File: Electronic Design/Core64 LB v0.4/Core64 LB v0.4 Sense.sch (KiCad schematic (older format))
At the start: 23 parts, among them U3 LM393

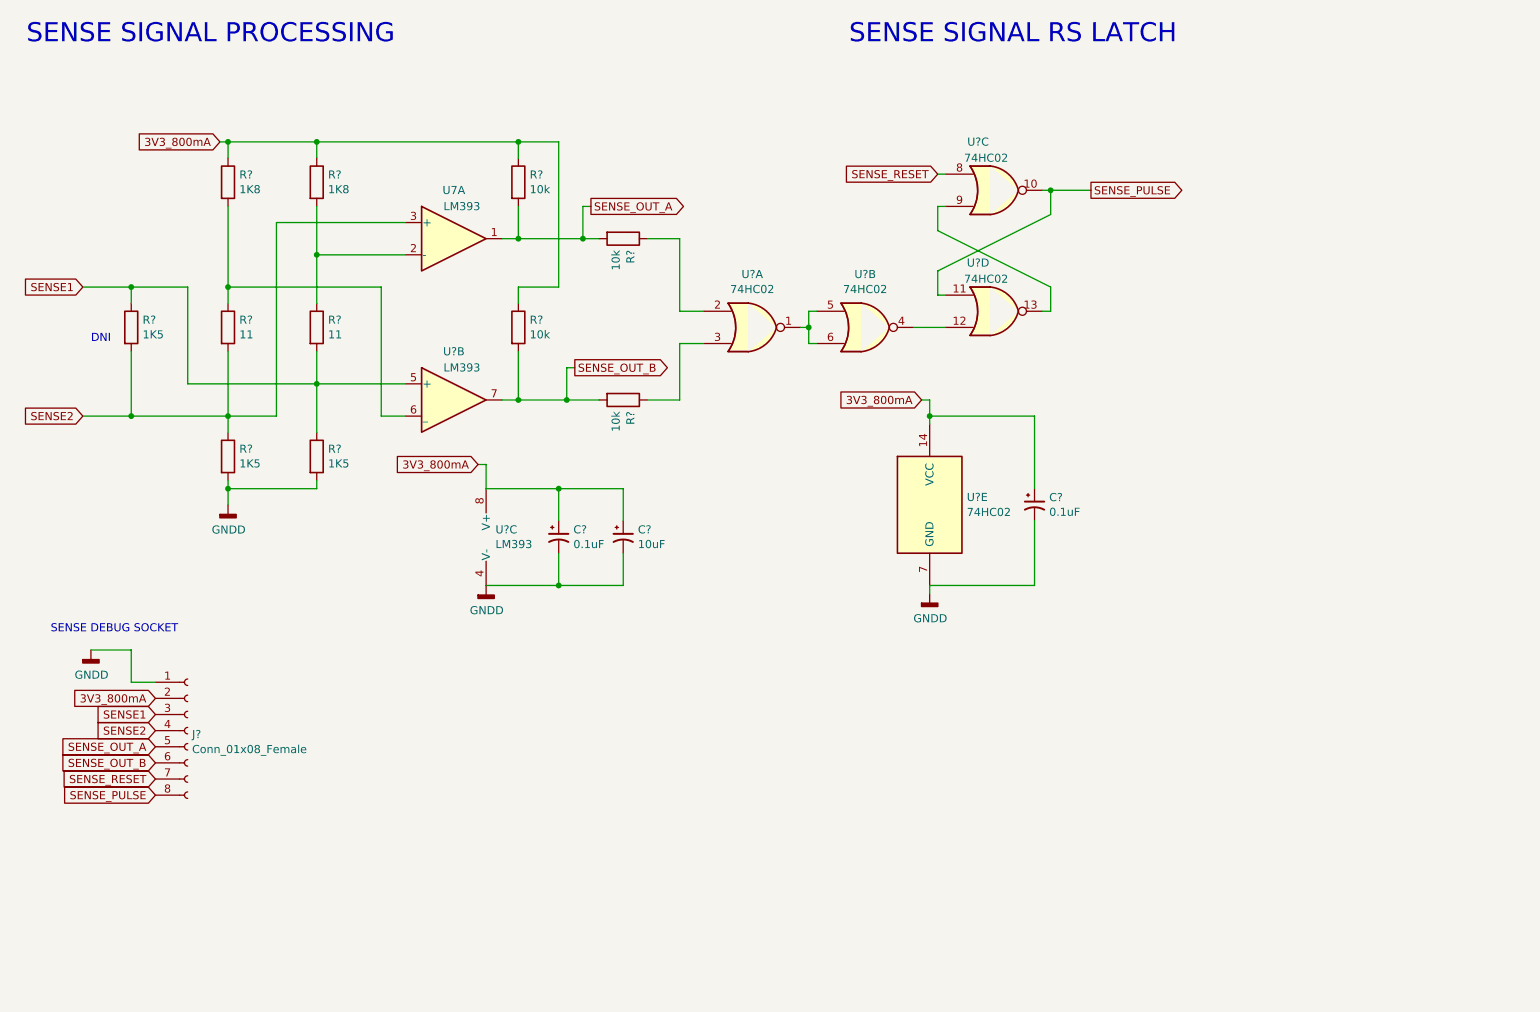
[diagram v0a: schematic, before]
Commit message: Correct Logic Board filenames to LB from CB
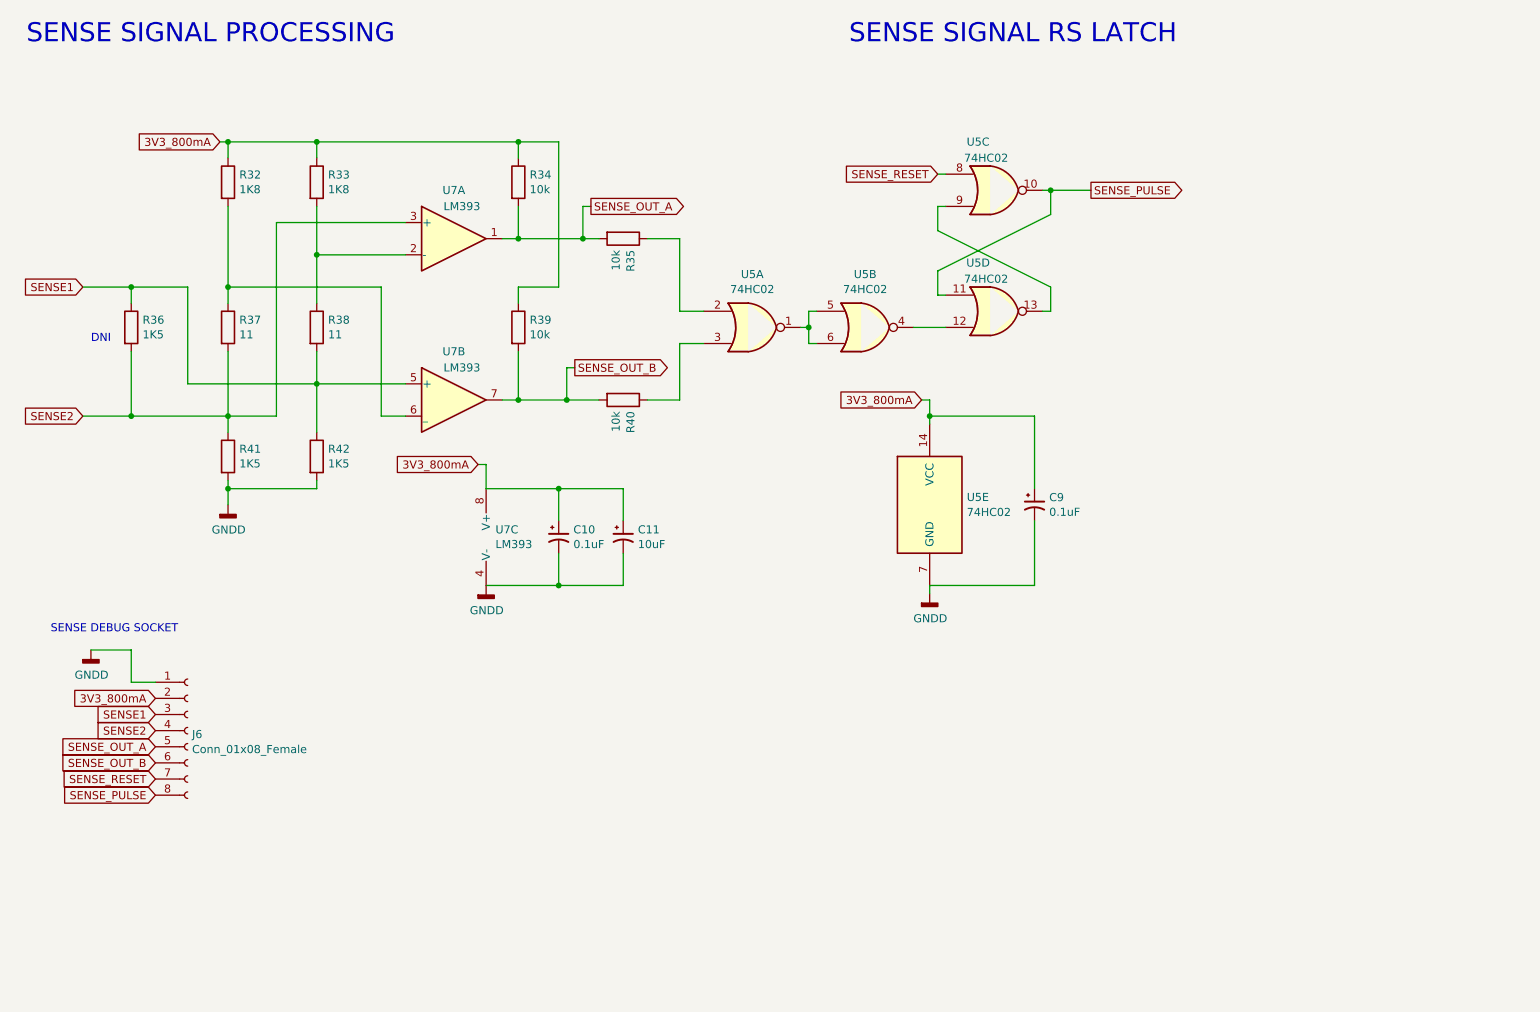
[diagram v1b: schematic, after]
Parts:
- gave numbers to parts that had none: 17
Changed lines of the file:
@@
 EESchema Schematic File Version 4
-LIBS:Core64 CB v0.4-cache
+LIBS:Core64 LB v0.4-cache
 EELAYER 29 0
 EELAYER END
@@
 SENSE2
 $Comp
-L Device:R R?
+L Device:R R32
 U 1 1 5D39C2B1
 P 1850 1700
-F 0 "R?" H 1920 1746 50  0000 L CNN
+F 0 "R32" H 1920 1746 50  0000 L CNN
 F 1 "1K8" H 1920 1655 50  0000 L CNN
 F 2 "Resistor_SMD:R_0805_2012Metric" V 1780 1700 50  0001 C CNN
@@
 $EndComp
 $Comp
-L Device:R R?
+L Device:R R33
 U 1 1 5D39F434
 P 2400 1700
-F 0 "R?" H 2470 1746 50  0000 L CNN
+F 0 "R33" H 2470 1746 50  0000 L CNN
 F 1 "1K8" H 2470 1655 50  0000 L CNN
 F 2 "Resistor_SMD:R_0805_2012Metric" V 2330 1700 50  0001 C CNN
@@
 $EndComp
 $Comp
-L Device:R R?
+L Device:R R37
 U 1 1 5D3A5EF4
 P 1850 2600
-F 0 "R?" H 1920 2646 50  0000 L CNN
+F 0 "R37" H 1920 2646 50  0000 L CNN
 F 1 "11" H 1920 2555 50  0000 L CNN
 F 2 "Resistor_SMD:R_0805_2012Metric" V 1780 2600 50  0001 C CNN
@@
 $EndComp
 $Comp
-L Device:R R?
+L Device:R R38
 U 1 1 5D3A668A
 P 2400 2600
-F 0 "R?" H 2470 2646 50  0000 L CNN
+F 0 "R38" H 2470 2646 50  0000 L CNN
 F 1 "11" H 2470 2555 50  0000 L CNN
 F 2 "Resistor_SMD:R_0805_2012Metric" V 2330 2600 50  0001 C CNN
@@
 $EndComp
 $Comp
-L Device:R R?
+L Device:R R41
 U 1 1 5D3A6BA6
 P 1850 3400
-F 0 "R?" H 1920 3446 50  0000 L CNN
+F 0 "R41" H 1920 3446 50  0000 L CNN
 F 1 "1K5" H 1920 3355 50  0000 L CNN
 F 2 "Resistor_SMD:R_0805_2012Metric" V 1780 3400 50  0001 C CNN
@@
 	2400 1850 2400 2150
 $Comp
-L power:GNDD #PWR?
+L power:GNDD #PWR0146
 U 1 1 5D3AE7CA
 P 1850 3700
-F 0 "#PWR?" H 1850 3450 50  0001 C CNN
+F 0 "#PWR0146" H 1850 3450 50  0001 C CNN
 F 1 "GNDD" H 1854 3545 50  0000 C CNN
 F 2 "" H 1850 3700 50  0001 C CNN
@@
 	1850 2350 1850 2450
 $Comp
-L Comparator:LM393 U?
+L Comparator:LM393 U7
 U 2 1 5D3C9C38
 P 3250 3050
-F 0 "U?" H 3250 3350 50  0000 C CNN
+F 0 "U7" H 3250 3350 50  0000 C CNN
 F 1 "LM393" H 3300 3250 50  0000 C CNN
 F 2 "Digikey:SOIC-8_W3.9mm" H 3250 3050 50  0001 C CNN
@@
 $EndComp
 $Comp
-L Comparator:LM393 U?
+L Comparator:LM393 U7
 U 3 1 5D3CAF67
 P 3550 3900
-F 0 "U?" H 3508 3946 50  0000 L CNN
+F 0 "U7" H 3508 3946 50  0000 L CNN
 F 1 "LM393" H 3508 3855 50  0000 L CNN
 F 2 "Digikey:SOIC-8_W3.9mm" H 3550 3900 50  0001 C CNN
@@
 $EndComp
 $Comp
-L power:GNDD #PWR?
+L power:GNDD #PWR0147
 U 1 1 5D3D5196
 P 3450 4200
-F 0 "#PWR?" H 3450 3950 50  0001 C CNN
+F 0 "#PWR0147" H 3450 3950 50  0001 C CNN
 F 1 "GNDD" H 3454 4045 50  0000 C CNN
 F 2 "" H 3450 4200 50  0001 C CNN
@@
 $EndComp
 $Comp
-L Device:R R?
+L Device:R R34
 U 1 1 5D3F592D
 P 3650 1700
-F 0 "R?" H 3720 1746 50  0000 L CNN
+F 0 "R34" H 3720 1746 50  0000 L CNN
 F 1 "10k" H 3720 1655 50  0000 L CNN
 F 2 "Resistor_SMD:R_0805_2012Metric" V 3580 1700 50  0001 C CNN
@@
 Connection ~ 1250 3150
 $Comp
-L Device:R R?
+L Device:R R36
 U 1 1 5D48BBA6
 P 1250 2600
-F 0 "R?" H 1320 2646 50  0000 L CNN
+F 0 "R36" H 1320 2646 50  0000 L CNN
 F 1 "1K5" H 1320 2555 50  0000 L CNN
 F 2 "Resistor_SMD:R_0805_2012Metric" V 1180 2600 50  0001 C CNN
@@
 	3550 3050 3650 3050
 $Comp
-L Device:R R?
+L Device:R R39
 U 1 1 5E624389
 P 3650 2600
-F 0 "R?" H 3720 2646 50  0000 L CNN
+F 0 "R39" H 3720 2646 50  0000 L CNN
 F 1 "10k" H 3720 2555 50  0000 L CNN
 F 2 "Resistor_SMD:R_0805_2012Metric" V 3580 2600 50  0001 C CNN
@@
 	3650 2050 4050 2050
 $Comp
-L Device:R R?
+L Device:R R40
 U 1 1 5E62BEBD
 P 4300 3050
-F 0 "R?" H 4370 3096 50  0000 L CNN
+F 0 "R40" H 4370 3096 50  0000 L CNN
 F 1 "10k" H 4370 3005 50  0000 L CNN
 F 2 "Resistor_SMD:R_0805_2012Metric" V 4230 3050 50  0001 C CNN
@@
 $EndComp
 $Comp
-L Device:R R?
+L Device:R R35
 U 1 1 5E631504
 P 4300 2050
-F 0 "R?" H 4370 2096 50  0000 L CNN
+F 0 "R35" H 4370 2096 50  0000 L CNN
 F 1 "10k" H 4370 2005 50  0000 L CNN
 F 2 "Resistor_SMD:R_0805_2012Metric" V 4230 2050 50  0001 C CNN
@@
 DNI
 $Comp
-L Device:CP1_Small C?
+L Device:CP1_Small C10
 U 1 1 5E6F58E8
 P 3900 3900
-F 0 "C?" H 3991 3946 50  0000 L CNN
+F 0 "C10" H 3991 3946 50  0000 L CNN
 F 1 "0.1uF" H 3991 3855 50  0000 L CNN
 F 2 "Capacitor_SMD:C_0805_2012Metric" H 3900 3900 50  0001 C CNN
@@
 $EndComp
 $Comp
-L Device:CP1_Small C?
+L Device:CP1_Small C11
 U 1 1 5E6F8864
 P 4300 3900
-F 0 "C?" H 4391 3946 50  0000 L CNN
+F 0 "C11" H 4391 3946 50  0000 L CNN
 F 1 "10uF" H 4391 3855 50  0000 L CNN
 F 2 "Capacitor_SMD:C_0805_2012Metric" H 4300 3900 50  0001 C CNN
@@
 SENSE_PULSE
 $Comp
-L 74xx:74HC02 U?
+L 74xx:74HC02 U5
 U 1 1 5E7CE53C
 P 5100 2600
-F 0 "U?" H 5100 2929 50  0000 C CNN
+F 0 "U5" H 5100 2929 50  0000 C CNN
 F 1 "74HC02" H 5100 2836 50  0000 C CNN
 F 2 "Package_SO:SOIC-14_3.9x8.7mm_P1.27mm" H 5100 2600 50  0001 C CNN
@@
 $EndComp
 $Comp
-L 74xx:74HC02 U?
+L 74xx:74HC02 U5
 U 2 1 5E7D6166
 P 5800 2600
-F 0 "U?" H 5800 2929 50  0000 C CNN
+F 0 "U5" H 5800 2929 50  0000 C CNN
 F 1 "74HC02" H 5800 2836 50  0000 C CNN
 F 2 "Package_SO:SOIC-14_3.9x8.7mm_P1.27mm" H 5800 2600 50  0001 C CNN
@@
 $EndComp
 $Comp
-L 74xx:74HC02 U?
+L 74xx:74HC02 U5
 U 3 1 5E7DA182
 P 6600 1750
-F 0 "U?" H 6500 2050 50  0000 C CNN
+F 0 "U5" H 6500 2050 50  0000 C CNN
 F 1 "74HC02" H 6550 1950 50  0000 C CNN
 F 2 "Package_SO:SOIC-14_3.9x8.7mm_P1.27mm" H 6600 1750 50  0001 C CNN
@@
 $EndComp
 $Comp
-L 74xx:74HC02 U?
+L 74xx:74HC02 U5
 U 4 1 5E7DD8C9
 P 6600 2500
-F 0 "U?" H 6500 2800 50  0000 C CNN
+F 0 "U5" H 6500 2800 50  0000 C CNN
 F 1 "74HC02" H 6550 2700 50  0000 C CNN
 F 2 "Package_SO:SOIC-14_3.9x8.7mm_P1.27mm" H 6600 2500 50  0001 C CNN
@@
 $EndComp
 $Comp
-L 74xx:74HC02 U?
+L 74xx:74HC02 U5
 U 5 1 5E7E6F63
 P 6200 3700
-F 0 "U?" H 6430 3747 50  0000 L CNN
+F 0 "U5" H 6430 3747 50  0000 L CNN
 F 1 "74HC02" H 6430 3654 50  0000 L CNN
 F 2 "Package_SO:SOIC-14_3.9x8.7mm_P1.27mm" H 6200 3700 50  0001 C CNN
@@
 	6100 2600 6300 2600
 $Comp
-L Device:CP1_Small C?
+L Device:CP1_Small C9
 U 1 1 5E84C4A5
 P 6850 3700
-F 0 "C?" H 6941 3746 50  0000 L CNN
+F 0 "C9" H 6941 3746 50  0000 L CNN
 F 1 "0.1uF" H 6941 3655 50  0000 L CNN
 F 2 "Capacitor_SMD:C_0805_2012Metric" H 6850 3700 50  0001 C CNN
@@
 	6850 4200 6200 4200
 $Comp
-L power:GNDD #PWR?
+L power:GNDD #PWR0148
 U 1 1 5E87D16F
 P 6200 4250
-F 0 "#PWR?" H 6200 4000 50  0001 C CNN
+F 0 "#PWR0148" H 6200 4000 50  0001 C CNN
 F 1 "GNDD" H 6204 4095 50  0000 C CNN
 F 2 "" H 6200 4250 50  0001 C CNN
@@
 	2400 1450 1850 1450
 $Comp
-L Connector:Conn_01x08_Female J?
+L Connector:Conn_01x08_Female J6
 U 1 1 5E868B9C
 P 1600 5100
-F 0 "J?" H 1627 5077 50  0000 L CNN
+F 0 "J6" H 1627 5077 50  0000 L CNN
 F 1 "Conn_01x08_Female" H 1627 4984 50  0000 L CNN
 F 2 "Connector_PinSocket_2.54mm:PinSocket_1x08_P2.54mm_Vertical" H 1600 5100 50  0001 C CNN
@@
 3V3_800mA
 $Comp
-L power:GNDD #PWR?
+L power:GNDD #PWR0149
 U 1 1 5E86E945
 P 1000 4600
-F 0 "#PWR?" H 1000 4350 50  0001 C CNN
+F 0 "#PWR0149" H 1000 4350 50  0001 C CNN
 F 1 "GNDD" H 1004 4445 50  0000 C CNN
 F 2 "" H 1000 4600 50  0001 C CNN
@@
 Connection ~ 2400 1450
 $Comp
-L Device:R R?
+L Device:R R42
 U 1 1 5D3A7392
 P 2400 3400
-F 0 "R?" H 2470 3446 50  0000 L CNN
+F 0 "R42" H 2470 3446 50  0000 L CNN
 F 1 "1K5" H 2470 3355 50  0000 L CNN
 F 2 "Resistor_SMD:R_0805_2012Metric" V 2330 3400 50  0001 C CNN

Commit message: Add regulator and battery connector data sheets, footprints, symbols
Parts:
- C10, C11, C9: symbol Device:CP1_Small -> Device:C
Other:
- note added: "All non-polarized capacitors are ceramic unless otherwise noted."
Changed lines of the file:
@@
 DNI
 $Comp
-L Device:CP1_Small C10
+L Device:C C10
 U 1 1 5E6F58E8
 P 3900 3900
@@
 $EndComp
 $Comp
-L Device:CP1_Small C11
+L Device:C C11
 U 1 1 5E6F8864
 P 4300 3900
@@
 $EndComp
 Wire Wire Line
-	4300 3600 4300 3800
+	4300 3600 4300 3750
 Wire Wire Line
 	3450 3600 3900 3600
 Wire Wire Line
-	3900 3600 3900 3800
+	3900 3600 3900 3750
 Connection ~ 3900 3600
 Wire Wire Line
@@
 	3450 4200 3900 4200
 Wire Wire Line
-	4300 4200 4300 4000
-Wire Wire Line
-	3900 4000 3900 4200
+	4300 4200 4300 4050
+Wire Wire Line
+	3900 4050 3900 4200
 Connection ~ 3900 4200
 Wire Wire Line
@@
 	6100 2600 6300 2600
 $Comp
-L Device:CP1_Small C9
+L Device:C C9
 U 1 1 5E84C4A5
 P 6850 3700
@@
 	3450 3600 3450 3450
 Wire Wire Line
-	6850 3150 6850 3600
-Wire Wire Line
-	6850 3800 6850 4200
+	6850 3150 6850 3550
+Wire Wire Line
+	6850 3850 6850 4200
 Wire Wire Line
 	6850 4200 6200 4200
@@
 	3900 1450 3650 1450
 Connection ~ 3650 1450
+Text Notes 6300 6750 0    50   ~ 0
+All non-polarized capacitors are ceramic unless otherwise noted.
 $EndSCHEMATC

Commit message: Complete LB power schematic, add 3-to-8 decoder
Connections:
- net 3V3_800mA renamed 3V3
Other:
- note added: "All non-polarized capacitors are X7R or X5R ceramic unless otherwise noted."
- note removed: "All non-polarized capacitors are ceramic unless otherwise noted."
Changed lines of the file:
@@
 U 1 1 5E62BEBD
 P 4300 3050
-F 0 "R40" H 4370 3096 50  0000 L CNN
-F 1 "10k" H 4370 3005 50  0000 L CNN
+F 0 "R40" V 4400 3000 50  0000 L CNN
+F 1 "10k" V 4500 3000 50  0000 L CNN
 F 2 "Resistor_SMD:R_0805_2012Metric" V 4230 3050 50  0001 C CNN
 F 3 "~" H 4300 3050 50  0001 C CNN
@@
 U 1 1 5E631504
 P 4300 2050
-F 0 "R35" H 4370 2096 50  0000 L CNN
-F 1 "10k" H 4370 2005 50  0000 L CNN
+F 0 "R35" V 4400 2000 50  0000 L CNN
+F 1 "10k" V 4500 2000 50  0000 L CNN
 F 2 "Resistor_SMD:R_0805_2012Metric" V 4230 2050 50  0001 C CNN
 F 3 "~" H 4300 2050 50  0001 C CNN
@@
 $EndComp
 Text GLabel 1800 1450 0    50   Input ~ 0
-3V3_800mA
+3V3
 Text GLabel 3400 3450 0    50   Input ~ 0
-3V3_800mA
+3V3
 Wire Wire Line
 	1850 1450 1850 1550
@@
 $EndComp
 Text GLabel 6150 3050 0    50   Input ~ 0
-3V3_800mA
+3V3
 Wire Wire Line
 	6200 3050 6200 3150
@@
 SENSE_PULSE
 Text GLabel 1400 4900 0    50   Input ~ 0
-3V3_800mA
+3V3
 $Comp
 L power:GNDD #PWR0149
@@
 Connection ~ 3650 1450
 Text Notes 6300 6750 0    50   ~ 0
-All non-polarized capacitors are ceramic unless otherwise noted.
+All non-polarized capacitors are X7R or X5R ceramic unless otherwise noted.
 $EndSCHEMATC
